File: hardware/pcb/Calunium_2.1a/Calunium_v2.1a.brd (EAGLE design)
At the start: 99.1 x 78.7 mm, 65 parts, among them IC1 MCP1702-3.3, IC2 DS1338, IC3 MCP1702-5.0, IC4 ATMEGA1284, IC5 MCP2200, Q1 2N7000, U1 CALUNIUM-SHIELD, X1 PWR, X2 JTAG, X3 USB, X4 CONN-SMATHD, X5 UART0, X6 MICRO-SD-SOCKETHIROSE-DM3D, Y1 32k768, Y2 16MHz, Y3 12MHz

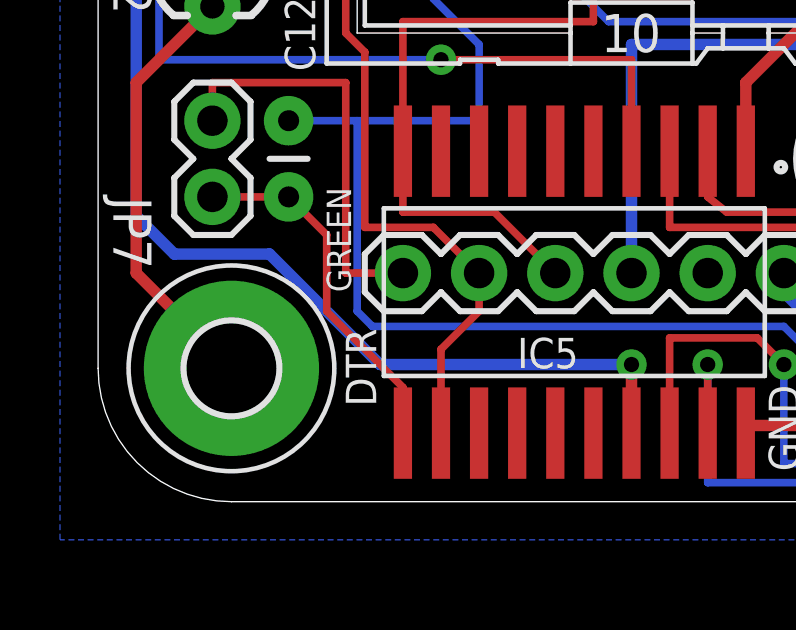
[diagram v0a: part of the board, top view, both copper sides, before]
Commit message: Fixing error where MCP2200 autoreset was not routed through JP7.
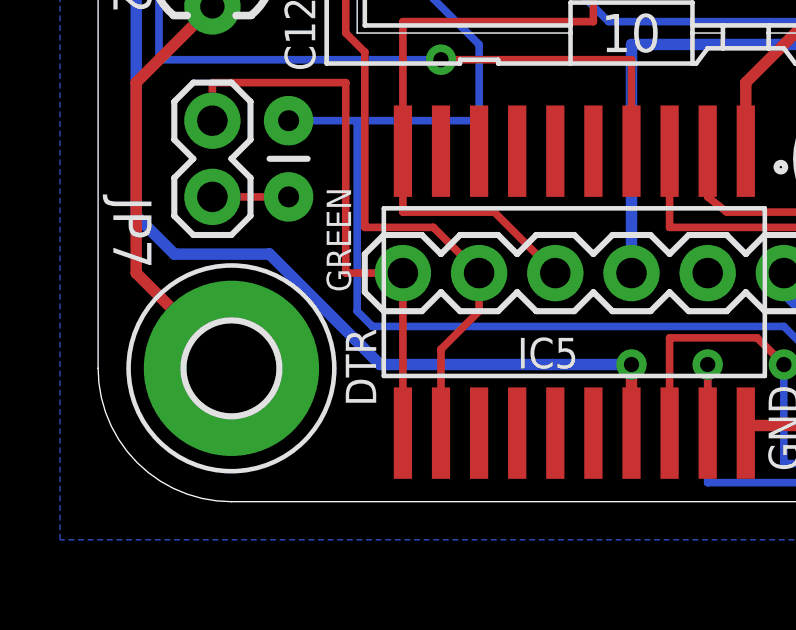
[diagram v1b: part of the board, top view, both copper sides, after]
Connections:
- net AUTO_RESET: now also JP7.1, X5.1; no longer C12.1, JP7.2
- net N$15: now also C12.1, JP7.2; no longer JP7.1, X5.1
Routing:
- net N$15: track 14.0 -> 2.54 mm
- net AUTO_RESET: track 12.1 -> 19.4 mm
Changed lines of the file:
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@@
 <?xml version="1.0" encoding="utf-8"?>
 <!DOCTYPE eagle SYSTEM "eagle.dtd">
-<eagle version="6.2">
+<eagle version="6.5.0">
 <drawing>
 <settings>
@@
 </class>
 </classes>
-<designrules>
+<designrules name="default">
 <description language="en">&lt;b&gt;EAGLE Design Rules&lt;/b&gt;
 &lt;p&gt;
@@
 <wire x1="71.12" y1="73.914" x2="68.072" y2="70.866" width="0.254" layer="16"/>
 </signal>
-<signal name="N$15">
+<signal name="AUTO_RESET">
+<contactref element="IC5" pad="11"/>
+<wire x1="10.16" y1="2.159" x2="10.16" y2="2.286" width="0.254" layer="1"/>
 <contactref element="X5" pad="1"/>
 <contactref element="JP7" pad="1"/>
@@
 <wire x1="8.255" y1="13.97" x2="3.81" y2="13.97" width="0.254" layer="1"/>
 <wire x1="3.81" y1="13.97" x2="3.81" y2="12.7" width="0.254" layer="1"/>
-</signal>
-<signal name="AUTO_RESET">
-<contactref element="JP7" pad="2"/>
-<contactref element="C12" pad="1"/>
-<wire x1="3.81" y1="10.16" x2="6.35" y2="10.16" width="0.254" layer="1"/>
-<contactref element="IC5" pad="11"/>
-<wire x1="10.16" y1="2.286" x2="10.16" y2="3.81" width="0.254" layer="1"/>
-<wire x1="10.16" y1="2.159" x2="10.16" y2="2.286" width="0.254" layer="1"/>
-<wire x1="10.16" y1="3.81" x2="7.62" y2="6.35" width="0.254" layer="1"/>
-<wire x1="7.62" y1="6.35" x2="7.62" y2="8.89" width="0.254" layer="1"/>
-<wire x1="7.62" y1="8.89" x2="6.35" y2="10.16" width="0.254" layer="1"/>
+<wire x1="10.16" y1="2.286" x2="10.16" y2="7.62" width="0.254" layer="1"/>
 </signal>
 <signal name="+3V3" class="1">
@@
 <wire x1="51.816" y1="51.562" x2="55.372" y2="51.562" width="0.254" layer="16"/>
 </signal>
+<signal name="N$15">
+<contactref element="JP7" pad="2"/>
+<contactref element="C12" pad="1"/>
+<wire x1="3.81" y1="10.16" x2="6.35" y2="10.16" width="0.254" layer="1"/>
+</signal>
 </signals>

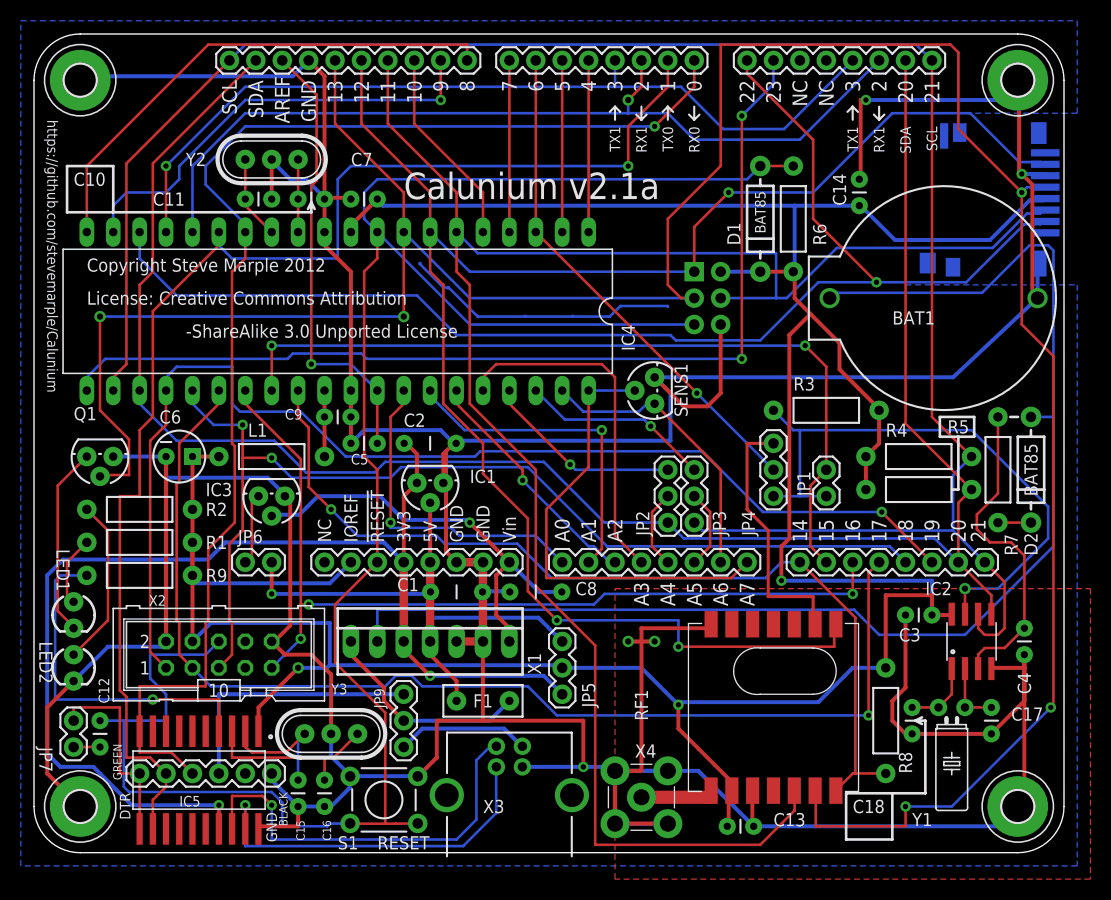
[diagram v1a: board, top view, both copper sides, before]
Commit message: Adding 1M pull-down resistor on D13.
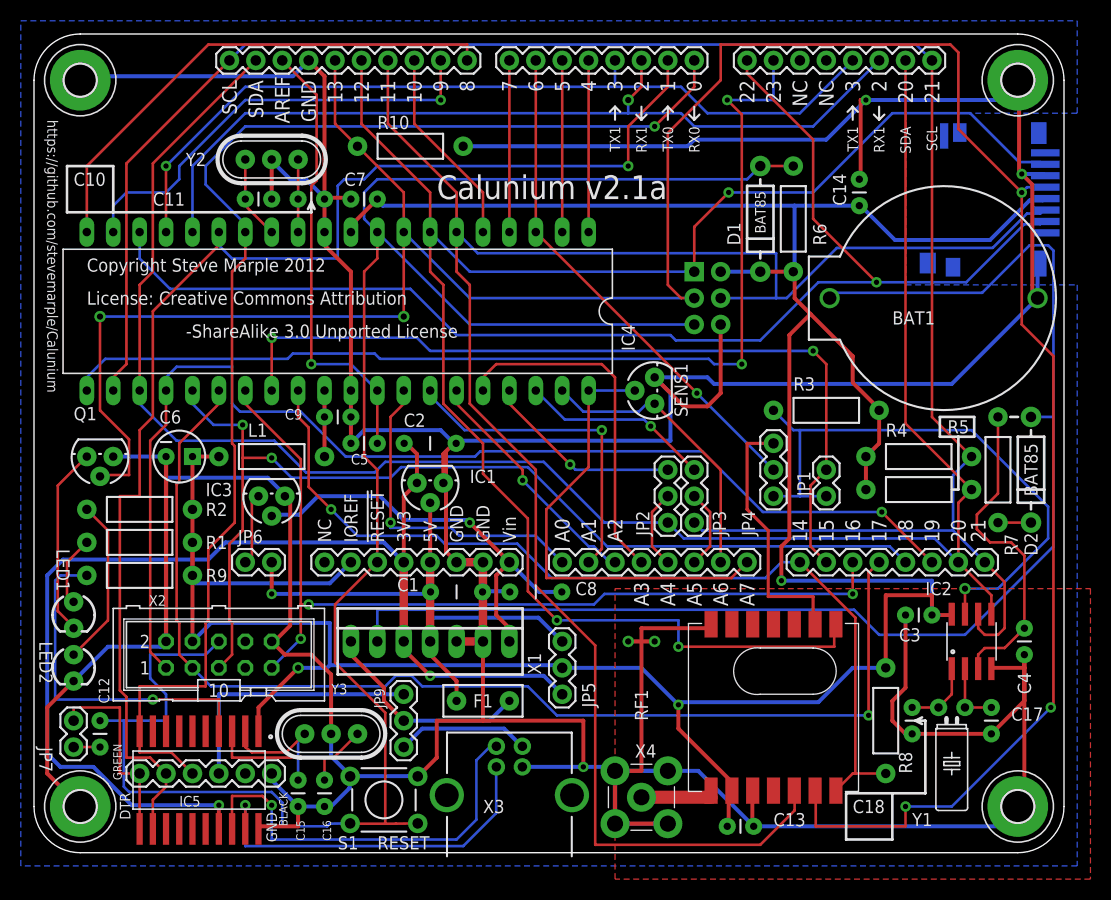
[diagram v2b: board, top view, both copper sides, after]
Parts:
- added R10: 1M, SteveMarple:RES-AXIAL-0.4
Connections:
- net 13(SCK): now also R10.P$2
- net GND: now also R10.P$1
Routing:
- net GND: track 549.4 -> 590.7 mm
- net GNDA: track 27.0 -> 0.00 mm
- net 23: track 95.4 -> 99.9 mm
- net 3(TX1): track 82.5 -> 81.2 mm
- net 15: track 78.6 -> 79.8 mm
- net 2(RX1): track 84.3 -> 83.3 mm

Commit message: Adding juumper to disconnect VCC from ISP header, routing improvements.
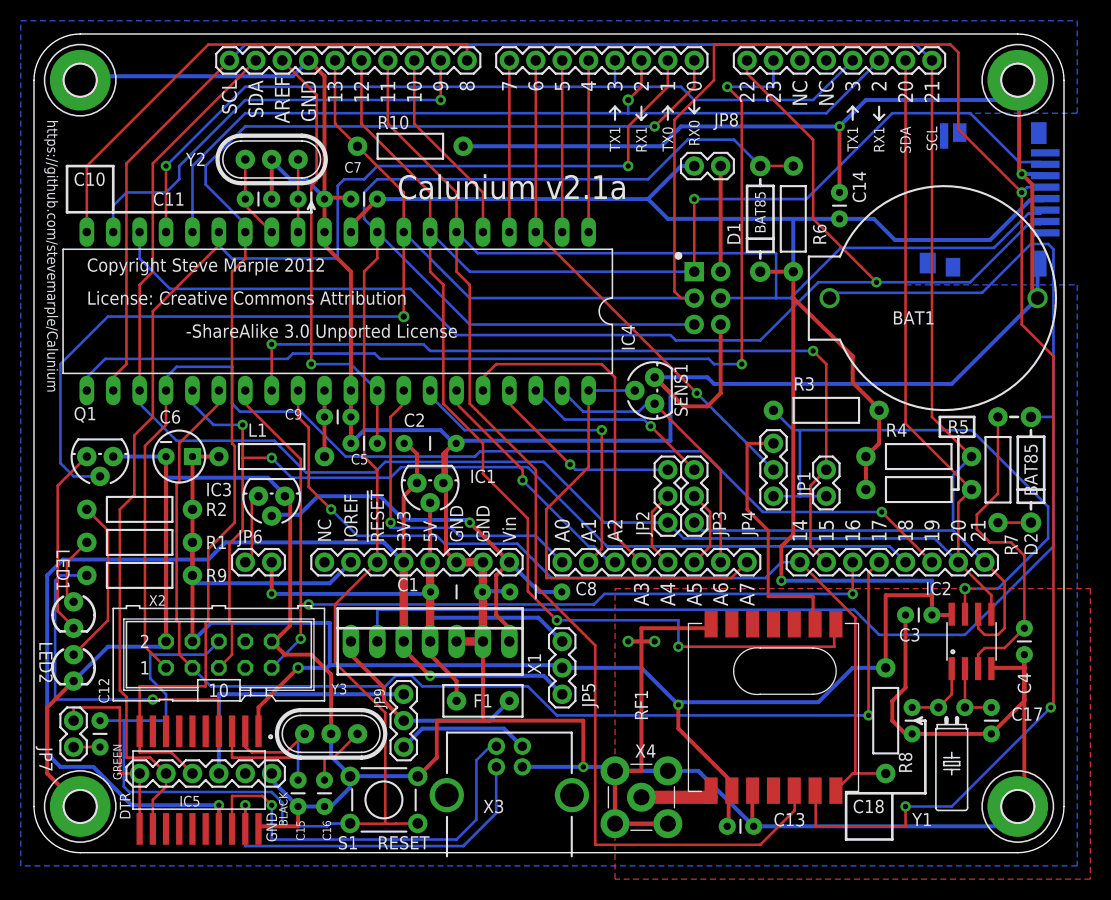
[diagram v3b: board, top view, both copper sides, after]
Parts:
- removed U1: CALUNIUM-SHIELD, SteveMarple:CALUNIUM-SHIELD-NO-OUTLINE-NO-HOLES-NO-TEXT-V2
- added JP8: ISP VCC, SparkFun:1X02
- added U$1: CALUNIUM-SHIELD-V3V3-NO-HOLES-NO-TEXT, SteveMarple:CALUNIUM-SHIELD-NO-OUTLINE-NO-HOLES-NO-TEXT-V3
- moved C14 2.29 mm to (77.5, 61.0)
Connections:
- removed net N$13: JP3.2, U1.A5/SCL
- new net A4/SDA: JP2.2, U$1.A4/SDA
- new net A5/SCL: JP3.2, U$1.A5/SCL
- net !RESET: now also U$1.!ISP_RESET, U$1.!RESET@0; no longer U1.!RESET@0, U1.!RESET@1
- net +3V3: now also U$1.3.3V; no longer U1.3.3V
- net +5V: now also U$1.5V; no longer U1.5V
- net 0(RX0): now also U$1.0(RX0); no longer U1.0(RX0)
- net 1(TX0): now also U$1.1(TX0); no longer U1.1(TX0)
- net 10: now also U$1.10; no longer U1.10
- net 11(MOSI): now also U$1.11@0, U$1.ISP_MOSI; no longer U1.11@0, U1.11@1
- net 12(MISO): now also U$1.12@0, U$1.ISP_MISO; no longer U1.12@0, U1.12@1
- net 13(SCK): now also U$1.13@0, U$1.ISP_SCK; no longer U1.13@0, U1.13@1
- net 14: now also U$1.14; no longer U1.14
- net 15: now also U$1.15; no longer U1.15
- net 16(TDI): now also U$1.16; no longer U1.16
- net 17(TDO): now also U$1.17; no longer U1.17
- net 18(TMS): now also U$1.18; no longer U1.18
- net 19(TCK): now also U$1.19; no longer U1.19
- net 2(RX1): now also U$1.2@0, U$1.2@1; no longer U1.2@0, U1.2@1
- net 20(SDA): now also U$1.20@0, U$1.20@1, U$1.SDA; no longer U1.20@0, U1.20@1, U1.SDA
- net 21(SCL): now also U$1.21@0, U$1.21@1, U$1.SCL; no longer U1.21@0, U1.21@1, U1.SCL
- net 22: now also U$1.22; no longer U1.22
- net 23: now also U$1.23; no longer U1.23
- net 3(TX1): now also U$1.3@0, U$1.3@1; no longer U1.3@0, U1.3@1
- net 4: now also U$1.4; no longer U1.4
- net 5: now also U$1.5; no longer U1.5
- net 6: now also U$1.6; no longer U1.6
- net 7: now also U$1.7; no longer U1.7
- net 8: now also U$1.8; no longer U1.8
- net 9: now also U$1.9; no longer U1.9
- net A0: now also U$1.A0; no longer U1.A0
- net A1: now also U$1.A1; no longer U1.A1
- net A2: now also U$1.A2; no longer U1.A2
- net A3: now also U$1.A3; no longer U1.A3
- net A6: now also U$1.A6; no longer U1.A6
- net A7: now also U$1.A7; no longer U1.A7
- net AREF: now also U$1.AREF; no longer U1.AREF
- net GND: now also U$1.GND@0, U$1.GND@1, U$1.GND@2, U$1.GND@3; no longer U1.GND@0, U1.GND@1, U1.GND@2, U1.GND@3
- net N$6: now also JP8.1, U$1.ISP_VCC; no longer JP2.2, U1.A4/SDA
- net VCC: now also JP8.2, U$1.IOREF; no longer U1.IOREF, U1.VCC
- net VIN: now also U$1.VIN; no longer U1.VIN
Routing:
- net N$13: track 7.61 -> 0.00 mm
- net A5/SCL: track 0.00 -> 7.61 mm
- net A4/SDA: track 0.00 -> 7.61 mm
- net N$6: track 7.61 -> 10.2 mm
- net !RESET: track 200.6 -> 202.7 mm
- net GND: track 590.7 -> 588.8 mm
- net 12(MISO): track 164.6 -> 166.2 mm
- net VCC: track 310.6 -> 311.9 mm
- net 1(TX0): track 126.8 -> 125.7 mm
- net 2(RX1): track 83.3 -> 82.2 mm
- net 3(TX1): track 81.2 -> 80.2 mm
- net 15: track 79.8 -> 78.9 mm
- net 13(SCK): track 259.3 -> 259.4 mm, vias 5 -> 4

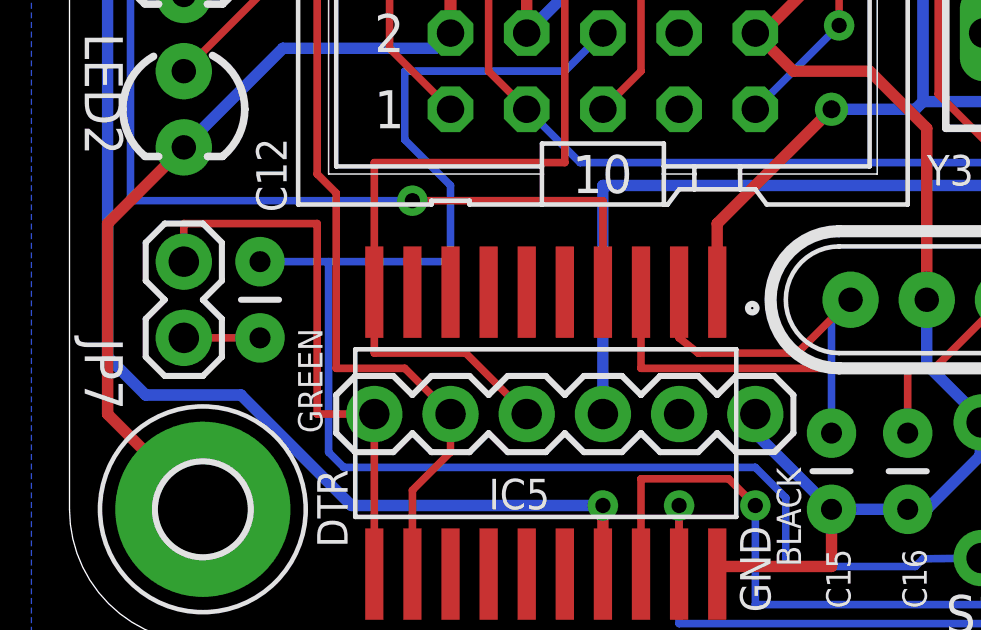
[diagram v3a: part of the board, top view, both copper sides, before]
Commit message: Minor routing changes to increase trace separation.
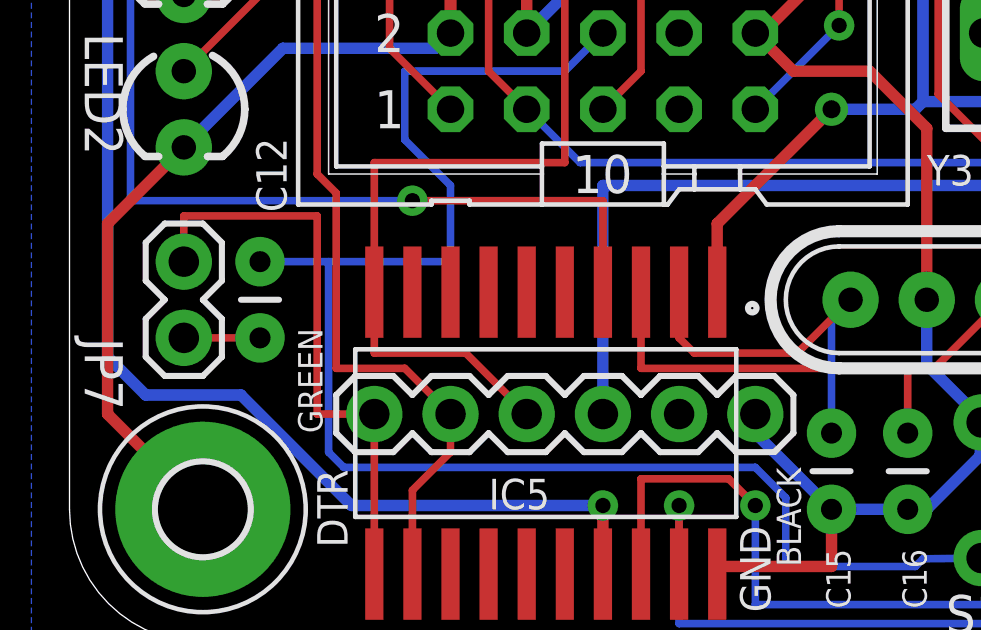
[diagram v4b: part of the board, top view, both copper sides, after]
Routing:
- net AUTO_RESET: track 19.4 -> 19.9 mm
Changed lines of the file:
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@@
 </class>
 </classes>
-<designrules name="default">
+<designrules name="SparkFun_Iteadstudio_10mil">
 <description language="en">&lt;b&gt;EAGLE Design Rules&lt;/b&gt;
 &lt;p&gt;
@@
 <contactref element="JP7" pad="1"/>
 <wire x1="10.16" y1="7.62" x2="8.255" y2="7.62" width="0.254" layer="1"/>
-<wire x1="8.255" y1="7.62" x2="8.255" y2="13.97" width="0.254" layer="1"/>
-<wire x1="8.255" y1="13.97" x2="3.81" y2="13.97" width="0.254" layer="1"/>
-<wire x1="3.81" y1="13.97" x2="3.81" y2="12.7" width="0.254" layer="1"/>
+<wire x1="8.255" y1="7.62" x2="8.255" y2="14.224" width="0.254" layer="1"/>
+<wire x1="8.255" y1="14.224" x2="3.81" y2="14.224" width="0.254" layer="1"/>
+<wire x1="3.81" y1="14.224" x2="3.81" y2="12.7" width="0.254" layer="1"/>
 <wire x1="10.16" y1="2.286" x2="10.16" y2="7.62" width="0.254" layer="1"/>
 </signal>
@@
 <contactref element="IC5" pad="2"/>
 <wire x1="26.035" y1="11.43" x2="24.257" y2="9.652" width="0.254" layer="1"/>
-<wire x1="24.257" y1="9.652" x2="20.955" y2="9.652" width="0.254" layer="1"/>
-<wire x1="20.955" y1="9.652" x2="20.32" y2="10.16" width="0.254" layer="1"/>
+<wire x1="24.257" y1="9.652" x2="20.828" y2="9.652" width="0.254" layer="1"/>
+<wire x1="20.828" y1="9.652" x2="20.32" y2="10.16" width="0.254" layer="1"/>
 <wire x1="20.32" y1="10.16" x2="20.32" y2="11.684" width="0.254" layer="1"/>
 <contactref element="C15" pad="1"/>
